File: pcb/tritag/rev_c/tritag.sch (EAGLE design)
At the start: 137 parts, among them J1 TC2030-JLINK-NL, J2 TC2030-JLINK-NL, J3 MICRO_USB_B_HIROSE_ZX62-B-5PA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, J4 BAT_HOLE, J5 BAT_HOLE, J7 CON_MICRO_SDDM3AT-SF-PEJM5, T1 HHM1595A1, U1 NRF52840, U12 SIP32510, U2 MCP73831, U3 FT232RQ, U4 MAX8887EZK33+T, U5 STM32F091CC, U6 SKY13317, U7 LXDC2HN18A, U8 DW1000, U9 LIS2DW12, X1 32MHz, X2 38.4M, X3 16M, X4 32.768kHz

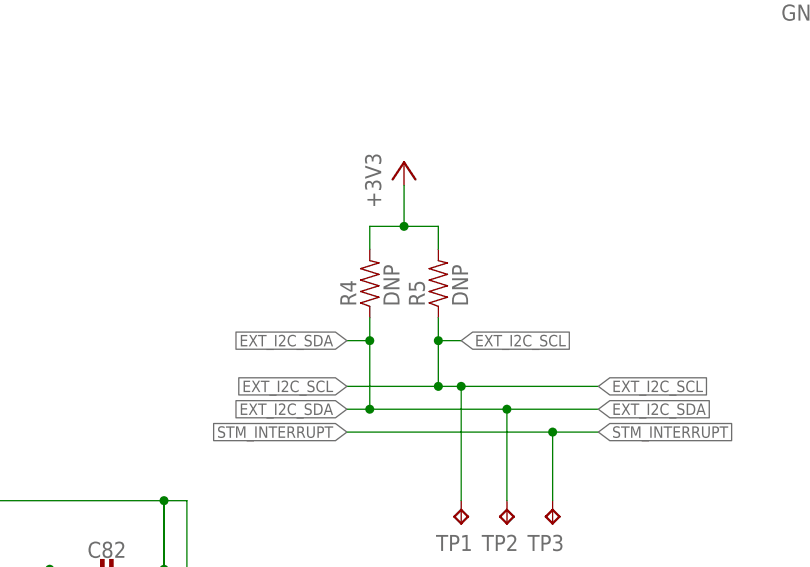
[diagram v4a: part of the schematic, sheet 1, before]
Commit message: Carrier ready for routing
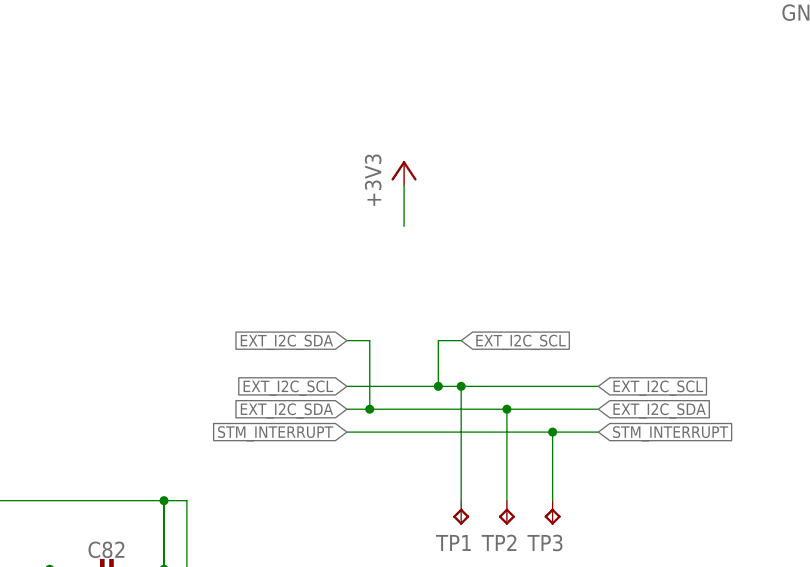
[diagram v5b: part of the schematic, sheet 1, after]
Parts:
- removed A2.1: TAIYO-YUDEN-AH086M, chips:TAIYO-YUDEN-AH086M
- removed J4: BAT_HOLE, connector:BAT_HOLE
- removed R4, R5: DNP, passives:RESISTOR0402_RES
- added A3: TAIYO-YUDEN-AH086M, chips:TAIYO-YUDEN-AH086M
- renumbered A5 to A1
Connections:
- removed net INTERRUPT: U5.PA2
- net +3V3: no longer R4.2, R5.2
- net EXT_I2C_SCL: no longer R5.1
- net EXT_I2C_SDA: no longer R4.1
- net GND: no longer J4.-
- net RF2: now also A2.ANTENNA; no longer A2.1.ANTENNA
- net RF3: now also A3.ANTENNA; no longer A2.ANTENNA
- net STM_INTERRUPT: now also U5.PA2
- net VBAT: no longer J4.+
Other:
- note added: "Do not use I2C pull-up (NRF has internal pull-up)"
- note removed: "Do Not Populate I2C pull-up (NRF has internal pull-up)"
- moved on the sheet: A2
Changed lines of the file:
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@@
 <part name="C11" library="passives" deviceset="CAPACITOR" device="0402_CAP" value="4.7uF"/>
 <part name="C9" library="passives" deviceset="CAPACITOR" device="0402_CAP" value="0.1uF"/>
-<part name="SUPPLY14" library="supply1" library_urn="urn:adsk.eagle:library:371" deviceset="GND" device=""/>
 <part name="SUPPLY3" library="supply1" library_urn="urn:adsk.eagle:library:371" deviceset="GND" device=""/>
 <part name="SUPPLY4" library="supply1" library_urn="urn:adsk.eagle:library:371" deviceset="GND" device=""/>
@@
 <part name="P+4" library="regulators" deviceset="+3V3" device=""/>
 <part name="GND5" library="supply1" library_urn="urn:adsk.eagle:library:371" deviceset="GND" device=""/>
-<part name="R4" library="passives" deviceset="RESISTOR" device="0402_RES" value="DNP"/>
-<part name="R5" library="passives" deviceset="RESISTOR" device="0402_RES" value="DNP"/>
 <part name="P+2" library="regulators" deviceset="+3V3" device=""/>
 <part name="D1" library="SparkFun-LED" deviceset="LED" device="0603" value="GREEN"/>
@@
 <part name="J3" library="connector" deviceset="MICRO_USB_B_HIROSE_ZX62-B-5PA(11)" device=""/>
 <part name="J5" library="connector" deviceset="BAT_HOLE" device=""/>
-<part name="J4" library="connector" deviceset="BAT_HOLE" device=""/>
 <part name="SUPPLY8" library="supply1" library_urn="urn:adsk.eagle:library:371" deviceset="GND" device=""/>
 <part name="TP2" library="testpad" library_urn="urn:adsk.eagle:library:385" deviceset="TP" device="TP06SQ" package3d_urn="urn:adsk.eagle:package:27952/1"/>
@@
 <part name="P+15" library="mote" deviceset="VSOL" device=""/>
 <part name="A4" library="chips" deviceset="ANT3216A063R2400A" device=""/>
+<part name="A3" library="chips" deviceset="TAIYO-YUDEN-AH086M" device=""/>
 <part name="A2" library="chips" deviceset="TAIYO-YUDEN-AH086M" device=""/>
-<part name="A2.1" library="chips" deviceset="TAIYO-YUDEN-AH086M" device=""/>
-<part name="A5" library="chips" deviceset="TAIYO-YUDEN-AH086M" device=""/>
+<part name="A1" library="chips" deviceset="TAIYO-YUDEN-AH086M" device=""/>
 <part name="C60" library="passives" deviceset="CAPACITOR" device="0402_CAP" value="820pF">
 <attribute name="DIGIKEY" value="445-1264-1-ND"/>
@@
 <plain>
 <text x="30.48" y="175.26" size="3.81" layer="98" align="bottom-center">nRF52840 BLE</text>
-<text x="210.82" y="93.98" size="1.778" layer="98">Do Not Populate I2C pull-up
+<text x="185.42" y="93.98" size="1.778" layer="98">Do not use I2C pull-up
 (NRF has internal pull-up)</text>
 <wire x1="177.8" y1="190.5" x2="177.8" y2="157.48" width="0.1524" layer="98" style="longdash"/>
@@
 <instance part="P+4" gate="P1" x="243.84" y="152.4"/>
 <instance part="GND5" gate="1" x="243.84" y="127"/>
-<instance part="R4" gate="G$1" x="195.58" y="96.52" rot="R90"/>
-<instance part="R5" gate="G$1" x="203.2" y="96.52" rot="R90"/>
 <instance part="P+2" gate="P1" x="199.39" y="108.712"/>
 <instance part="TP2" gate="G$1" x="210.82" y="68.58" rot="R180"/>
@@
 </segment>
 <segment>
-<pinref part="R4" gate="G$1" pin="2"/>
-<wire x1="195.58" y1="99.06" x2="195.58" y2="101.6" width="0.1524" layer="91"/>
-<pinref part="R5" gate="G$1" pin="2"/>
-<wire x1="195.58" y1="101.6" x2="199.39" y2="101.6" width="0.1524" layer="91"/>
-<wire x1="199.39" y1="101.6" x2="203.2" y2="101.6" width="0.1524" layer="91"/>
-<wire x1="203.2" y1="101.6" x2="203.2" y2="99.06" width="0.1524" layer="91"/>
 <pinref part="P+2" gate="P1" pin="+3V3"/>
 <wire x1="199.39" y1="101.6" x2="199.39" y2="106.172" width="0.1524" layer="91"/>
-<junction x="199.39" y="101.6"/>
 </segment>
 <segment>
@@
 <segment>
 <label x="193.04" y="81.28" size="1.27" layer="95" rot="R180" xref="yes"/>
-<pinref part="R4" gate="G$1" pin="1"/>
-<wire x1="195.58" y1="91.44" x2="195.58" y2="88.9" width="0.1524" layer="91"/>
 <wire x1="195.58" y1="88.9" x2="193.04" y2="88.9" width="0.1524" layer="91"/>
 <label x="193.04" y="88.9" size="1.27" layer="95" rot="R180" xref="yes"/>
@@
 <wire x1="210.82" y1="81.28" x2="220.98" y2="81.28" width="0.1524" layer="91"/>
 <wire x1="195.58" y1="88.9" x2="195.58" y2="81.28" width="0.1524" layer="91"/>
-<junction x="195.58" y="88.9"/>
 <junction x="195.58" y="81.28"/>
 <pinref part="TP2" gate="G$1" pin="TP"/>
@@
 <segment>
 <label x="193.04" y="83.82" size="1.27" layer="95" rot="R180" xref="yes"/>
-<pinref part="R5" gate="G$1" pin="1"/>
-<wire x1="203.2" y1="91.44" x2="203.2" y2="88.9" width="0.1524" layer="91"/>
 <wire x1="203.2" y1="88.9" x2="205.74" y2="88.9" width="0.1524" layer="91"/>
 <label x="205.74" y="88.9" size="1.27" layer="95" xref="yes"/>
@@
 <wire x1="203.2" y1="83.82" x2="193.04" y2="83.82" width="0.1524" layer="91"/>
 <wire x1="203.2" y1="88.9" x2="203.2" y2="83.82" width="0.1524" layer="91"/>
-<junction x="203.2" y="88.9"/>
 <junction x="203.2" y="83.82"/>
 <pinref part="TP1" gate="G$1" pin="TP"/>
@@
 <attribute name="VALUE" x="186.69" y="136.779" size="1.778" layer="96" rot="R180"/>
 </instance>
-<instance part="SUPPLY14" gate="1" x="162.56" y="165.1"/>
 <instance part="SUPPLY3" gate="1" x="71.12" y="127"/>
 <instance part="SUPPLY4" gate="1" x="170.18" y="127"/>
@@
 <instance part="J3" gate="G$1" x="50.8" y="152.4" rot="MR0"/>
 <instance part="J5" gate="G$1" x="190.5" y="175.26" rot="MR0"/>
-<instance part="J4" gate="G$1" x="147.32" y="175.26"/>
 <instance part="SUPPLY8" gate="1" x="177.8" y="165.1"/>
 <instance part="U4" gate="G$1" x="218.44" y="157.48"/>
@@
 <instance part="R22" gate="G$1" x="88.9" y="40.64" rot="R90"/>
 <instance part="R23" gate="G$1" x="101.6" y="40.64" rot="R90"/>
-<instance part="A2" gate="G$1" x="129.54" y="86.36"/>
-<instance part="A2.1" gate="G$1" x="119.38" y="88.9"/>
-<instance part="A5" gate="G$1" x="109.22" y="91.44"/>
+<instance part="A3" gate="G$1" x="129.54" y="86.36"/>
+<instance part="A2" gate="G$1" x="119.38" y="88.9"/>
+<instance part="A1" gate="G$1" x="109.22" y="91.44"/>
 </instances>
 <busses>
@@
 <pinref part="SUPPLY2" gate="1" pin="GND"/>
 <wire x1="157.48" y1="129.54" x2="157.48" y2="139.7" width="0.1524" layer="91"/>
-</segment>
-<segment>
-<pinref part="SUPPLY14" gate="1" pin="GND"/>
-<wire x1="162.56" y1="172.72" x2="162.56" y2="167.64" width="0.1524" layer="91"/>
-<pinref part="J4" gate="G$1" pin="-"/>
-<wire x1="157.48" y1="172.72" x2="162.56" y2="172.72" width="0.1524" layer="91"/>
 </segment>
 <segment>
@@
 <junction x="200.66" y="160.02"/>
 <wire x1="170.18" y1="177.8" x2="170.18" y2="160.02" width="0.1524" layer="91"/>
-<pinref part="J4" gate="G$1" pin="+"/>
-<wire x1="170.18" y1="177.8" x2="157.48" y2="177.8" width="0.1524" layer="91"/>
 <pinref part="J5" gate="G$1" pin="+"/>
 <wire x1="170.18" y1="177.8" x2="180.34" y2="177.8" width="0.1524" layer="91"/>
-<junction x="170.18" y="177.8"/>
 <pinref part="U4" gate="G$1" pin="IN"/>
 <wire x1="200.66" y1="160.02" x2="205.74" y2="160.02" width="0.1524" layer="91"/>
@@
 <wire x1="144.78" y1="157.48" x2="144.78" y2="160.02" width="0.1524" layer="91"/>
 <junction x="144.78" y="160.02"/>
-<label x="170.18" y="177.8" size="1.778" layer="95"/>
+<label x="170.18" y="177.8" size="1.778" layer="95" rot="MR0"/>
 </segment>
 </net>
@@
 <net name="RF1" class="0">
 <segment>
-<pinref part="A5" gate="G$1" pin="ANTENNA"/>
+<pinref part="A1" gate="G$1" pin="ANTENNA"/>
 <wire x1="106.68" y1="78.74" x2="109.22" y2="78.74" width="0.1524" layer="91"/>
 <wire x1="109.22" y1="78.74" x2="109.22" y2="86.36" width="0.1524" layer="91"/>
@@
 <net name="RF2" class="0">
 <segment>
-<pinref part="A2.1" gate="G$1" pin="ANTENNA"/>
+<pinref part="A2" gate="G$1" pin="ANTENNA"/>
 <wire x1="106.68" y1="73.66" x2="119.38" y2="73.66" width="0.1524" layer="91"/>
 <wire x1="119.38" y1="73.66" x2="119.38" y2="83.82" width="0.1524" layer="91"/>
@@
 <net name="RF3" class="0">
 <segment>
-<pinref part="A2" gate="G$1" pin="ANTENNA"/>
+<pinref part="A3" gate="G$1" pin="ANTENNA"/>
 <wire x1="106.68" y1="68.58" x2="129.54" y2="68.58" width="0.1524" layer="91"/>
 <wire x1="129.54" y1="68.58" x2="129.54" y2="81.28" width="0.1524" layer="91"/>
@@
 </segment>
 </net>
-<net name="INTERRUPT" class="0">
+<net name="STM_INTERRUPT" class="0">
 <segment>
 <wire x1="53.34" y1="132.08" x2="93.98" y2="132.08" width="0.1524" layer="91"/>
@@
 </segment>
 </net>
-<net name="INTERRUPT" class="0">
+<net name="RF1" class="0">
+<segment>
+<wire x1="35.56" y1="101.6" x2="50.8" y2="101.6" width="0.1524" layer="91"/>
+<label x="50.8" y="101.6" size="2.54" layer="95" xref="yes"/>
+</segment>
+</net>
+<net name="RF2" class="0">
+<segment>
+<wire x1="35.56" y1="96.52" x2="50.8" y2="96.52" width="0.1524" layer="91"/>
+<label x="50.8" y="96.52" size="2.54" layer="95" xref="yes"/>
+</segment>
+</net>
+<net name="RF3" class="0">
+<segment>
+<wire x1="35.56" y1="91.44" x2="50.8" y2="91.44" width="0.1524" layer="91"/>
+<label x="50.8" y="91.44" size="2.54" layer="95" xref="yes"/>
+</segment>
+</net>
+<net name="+3V3" class="0">
+<segment>
+<wire x1="35.56" y1="71.12" x2="50.8" y2="71.12" width="0.1524" layer="91"/>
+<label x="50.8" y="71.12" size="2.54" layer="95" xref="yes"/>
+</segment>
+</net>
+<net name="STM_INTERRUPT" class="0">
 <segment>
 <wire x1="35.56" y1="116.84" x2="50.8" y2="116.84" width="0.1524" layer="91"/>
@@
 </segment>
 </net>
-<net name="RF1" class="0">
-<segment>
-<wire x1="35.56" y1="101.6" x2="50.8" y2="101.6" width="0.1524" layer="91"/>
-<label x="50.8" y="101.6" size="2.54" layer="95" xref="yes"/>
-</segment>
-</net>
-<net name="RF2" class="0">
-<segment>
-<wire x1="35.56" y1="96.52" x2="50.8" y2="96.52" width="0.1524" layer="91"/>
-<label x="50.8" y="96.52" size="2.54" layer="95" xref="yes"/>
-</segment>
-</net>
-<net name="RF3" class="0">
-<segment>
-<wire x1="35.56" y1="91.44" x2="50.8" y2="91.44" width="0.1524" layer="91"/>
-<label x="50.8" y="91.44" size="2.54" layer="95" xref="yes"/>
-</segment>
-</net>
-<net name="+3V3" class="0">
-<segment>
-<wire x1="35.56" y1="71.12" x2="50.8" y2="71.12" width="0.1524" layer="91"/>
-<label x="50.8" y="71.12" size="2.54" layer="95" xref="yes"/>
-</segment>
-</net>

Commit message: carrier board finalized, HW revision completed
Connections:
- removed net !RST: U1.P0.18, U3.!RESET
- removed net NRF_SWO: J1.SWO, U1.P1.00
- removed net SCK: U1.P0.12
- removed net VSEC: U1.P0.31/AIN7
- removed net VSOL: U1.P0.30/AIN6
- new net !FT_RST: U1.P1.08, U3.!RESET
- net !NRF_CS_IMU: now also U1.P0.16; no longer U1.P0.21
- net !NRF_CS_SD: now also U1.P0.18; no longer U1.P0.19
- net !SD_DETECT: now also U1.P1.00; no longer U1.P0.24
- net BATIN: no longer U1.P1.07
- net DBG_RX: now also U1.P0.07; no longer U1.P0.26
- net DBG_TX: now also U1.P0.11; no longer U1.P0.27
- net EXT_I2C_SCL: now also U1.P1.09; no longer U1.P0.13
- net EXT_I2C_SDA: now also U1.P0.12; no longer U1.P0.15
- net LED_NRF_BLUE: now also U1.P0.04/AIN2; no longer U1.P0.05/AIN3
- net LED_NRF_RED: now also U1.P0.05/AIN3; no longer U1.P0.04/AIN2
- net NRF_GPIO_0: now also U1.P0.27; no longer U1.P0.16
- net NRF_GPIO_1: now also U1.P0.26; no longer U1.P0.17
- net NRF_IMU_INT1: now also U1.P0.22; no longer U1.P0.20
- net NRF_IMU_INT2: now also U1.P0.24; no longer U1.P0.22
- net NRF_MISO: now also U1.P0.15; no longer U1.P1.09
- net NRF_MOSI: now also U1.P0.13; no longer U1.P0.08
- net NRF_SCK: now also U1.P0.17
- net SD_EN: now also U1.P0.14; no longer U1.P0.23
- net STM_INTERRUPT: now also U1.P0.08; no longer U1.P0.25
- net VBAT: no longer U1.P0.29/AIN5
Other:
- moved on the sheet: TP13, TP14

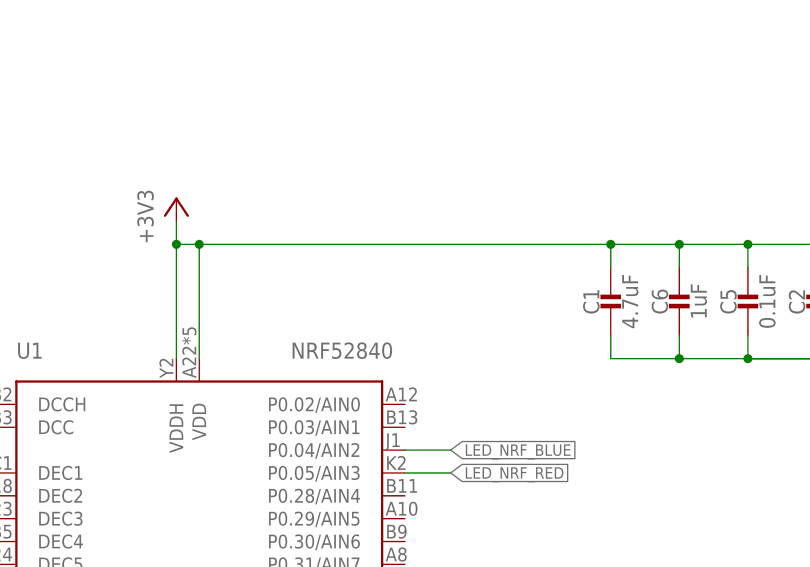
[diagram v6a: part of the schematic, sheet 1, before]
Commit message: added antenna keepout, improved power distribution and ground coverage plus RF for nRF
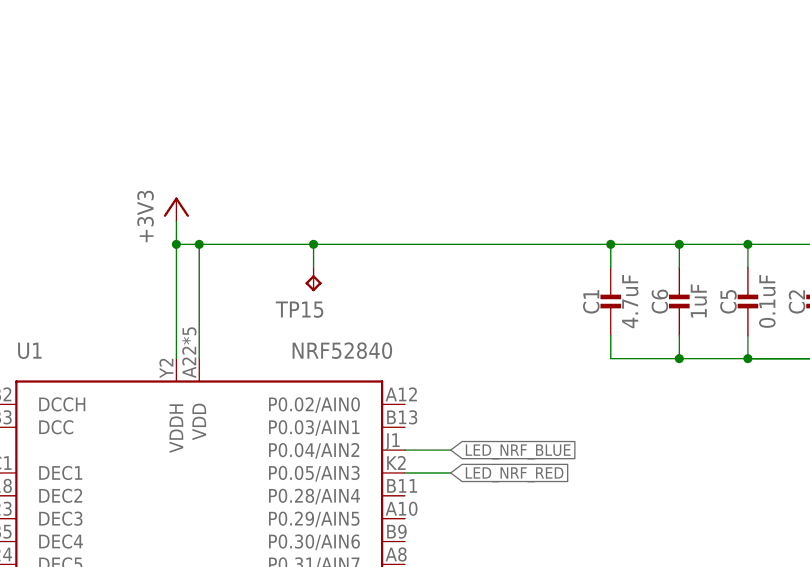
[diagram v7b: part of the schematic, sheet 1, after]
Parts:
- added TP15: TPTP06SQ, testpad:TPTP06SQ
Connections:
- net +3V3: now also TP15.TP
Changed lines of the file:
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@@
 <part name="TP11" library="headers" deviceset="TEST-POINT" device=""/>
 <part name="TP12" library="headers" deviceset="TEST-POINT" device=""/>
+<part name="TP15" library="testpad" library_urn="urn:adsk.eagle:library:385" deviceset="TP" device="TP06SQ" package3d_urn="urn:adsk.eagle:package:27952/1"/>
 </parts>
 <sheets>
@@
 <instance part="TP13" gate="G$1" x="121.92" y="68.58" rot="R180"/>
 <instance part="TP14" gate="G$1" x="121.92" y="66.04" rot="R180"/>
+<instance part="TP15" gate="G$1" x="96.52" y="144.78" rot="R180"/>
 </instances>
 <busses>
@@
 <segment>
 <pinref part="C1" gate="G$1" pin="1"/>
-<wire x1="83.82" y1="149.86" x2="129.54" y2="149.86" width="0.1524" layer="91"/>
+<wire x1="83.82" y1="149.86" x2="96.52" y2="149.86" width="0.1524" layer="91"/>
+<wire x1="96.52" y1="149.86" x2="129.54" y2="149.86" width="0.1524" layer="91"/>
 <wire x1="129.54" y1="149.86" x2="129.54" y2="147.32" width="0.1524" layer="91"/>
 <wire x1="129.54" y1="149.86" x2="137.16" y2="149.86" width="0.1524" layer="91"/>
@@
 <wire x1="81.28" y1="152.4" x2="81.28" y2="149.86" width="0.1524" layer="91"/>
 <junction x="81.28" y="149.86"/>
+<pinref part="TP15" gate="G$1" pin="TP"/>
+<wire x1="96.52" y1="147.32" x2="96.52" y2="149.86" width="0.1524" layer="91"/>
+<junction x="96.52" y="149.86"/>
 </segment>
 </net>
